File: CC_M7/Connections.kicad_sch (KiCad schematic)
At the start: 11 parts, among them J11 USB_B_Micro, J12 Conn_01x05_Pin, J16 Conn_01x06_Pin, J17 Conn_01x04_Pin, J3 Conn_01x03_Pin, J4 Conn_01x03_Pin, J5 Conn_01x03_Pin, J6 Conn_01x03_Pin, J7 Conn_01x03_Pin, J8 Conn_01x03_Pin

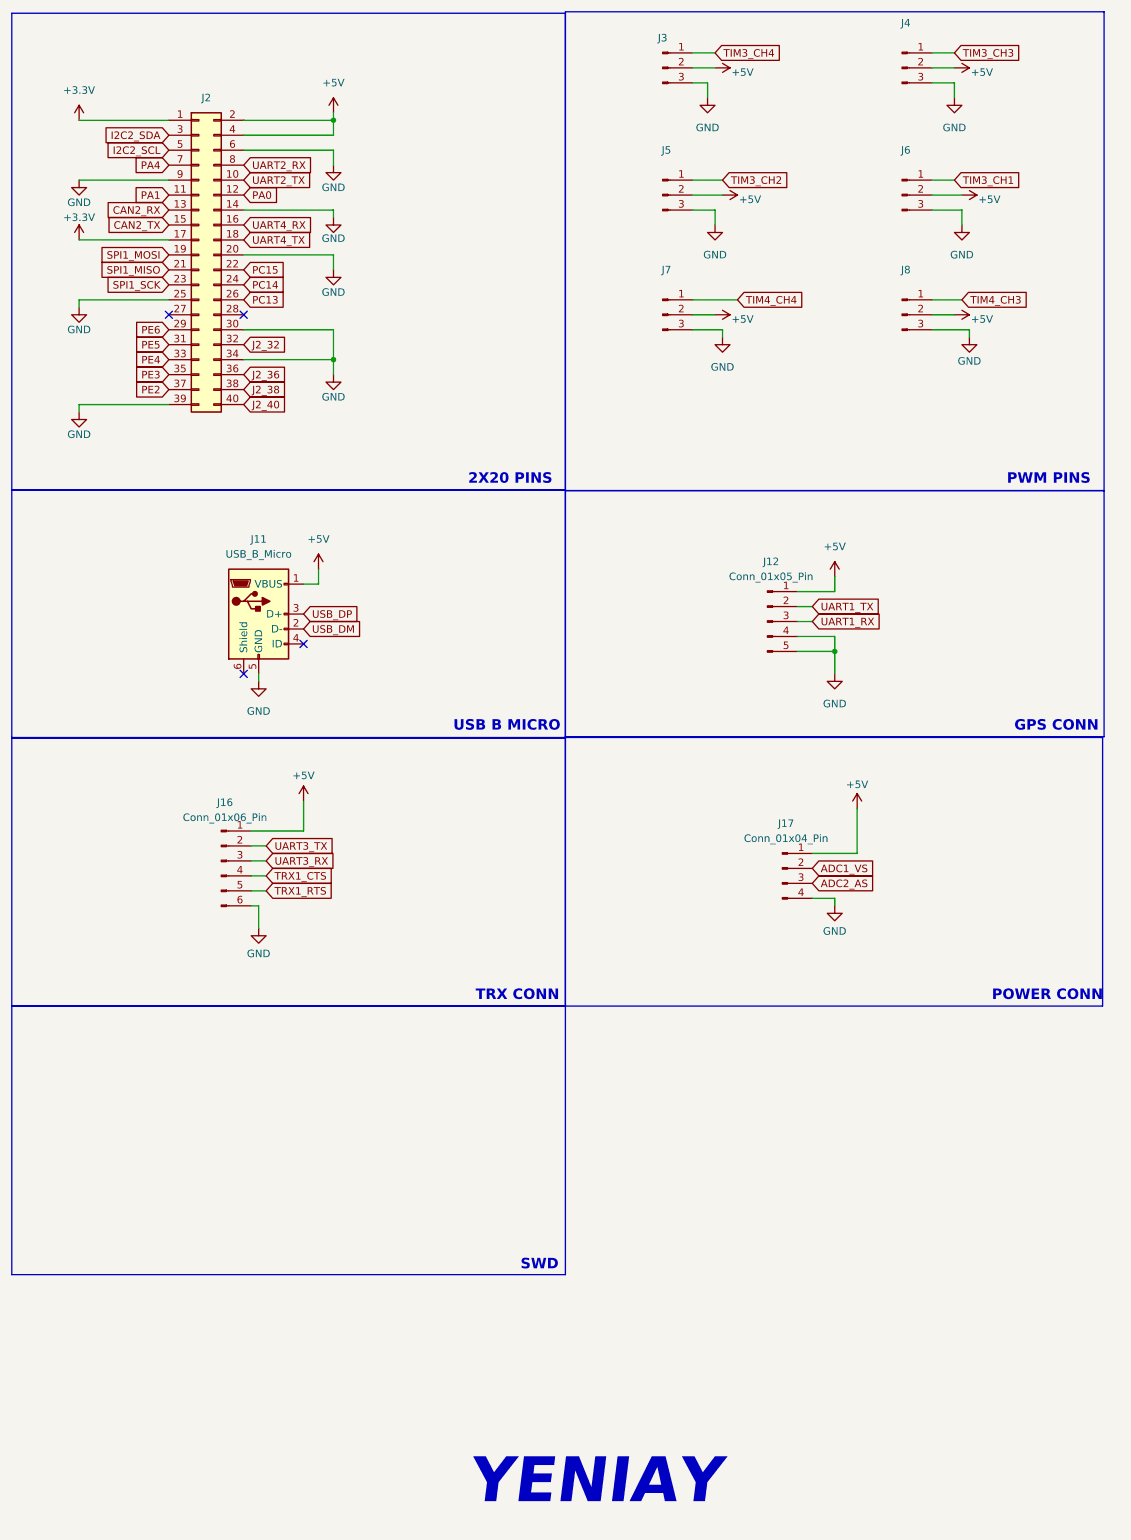
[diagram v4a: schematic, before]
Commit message: schematic control comment
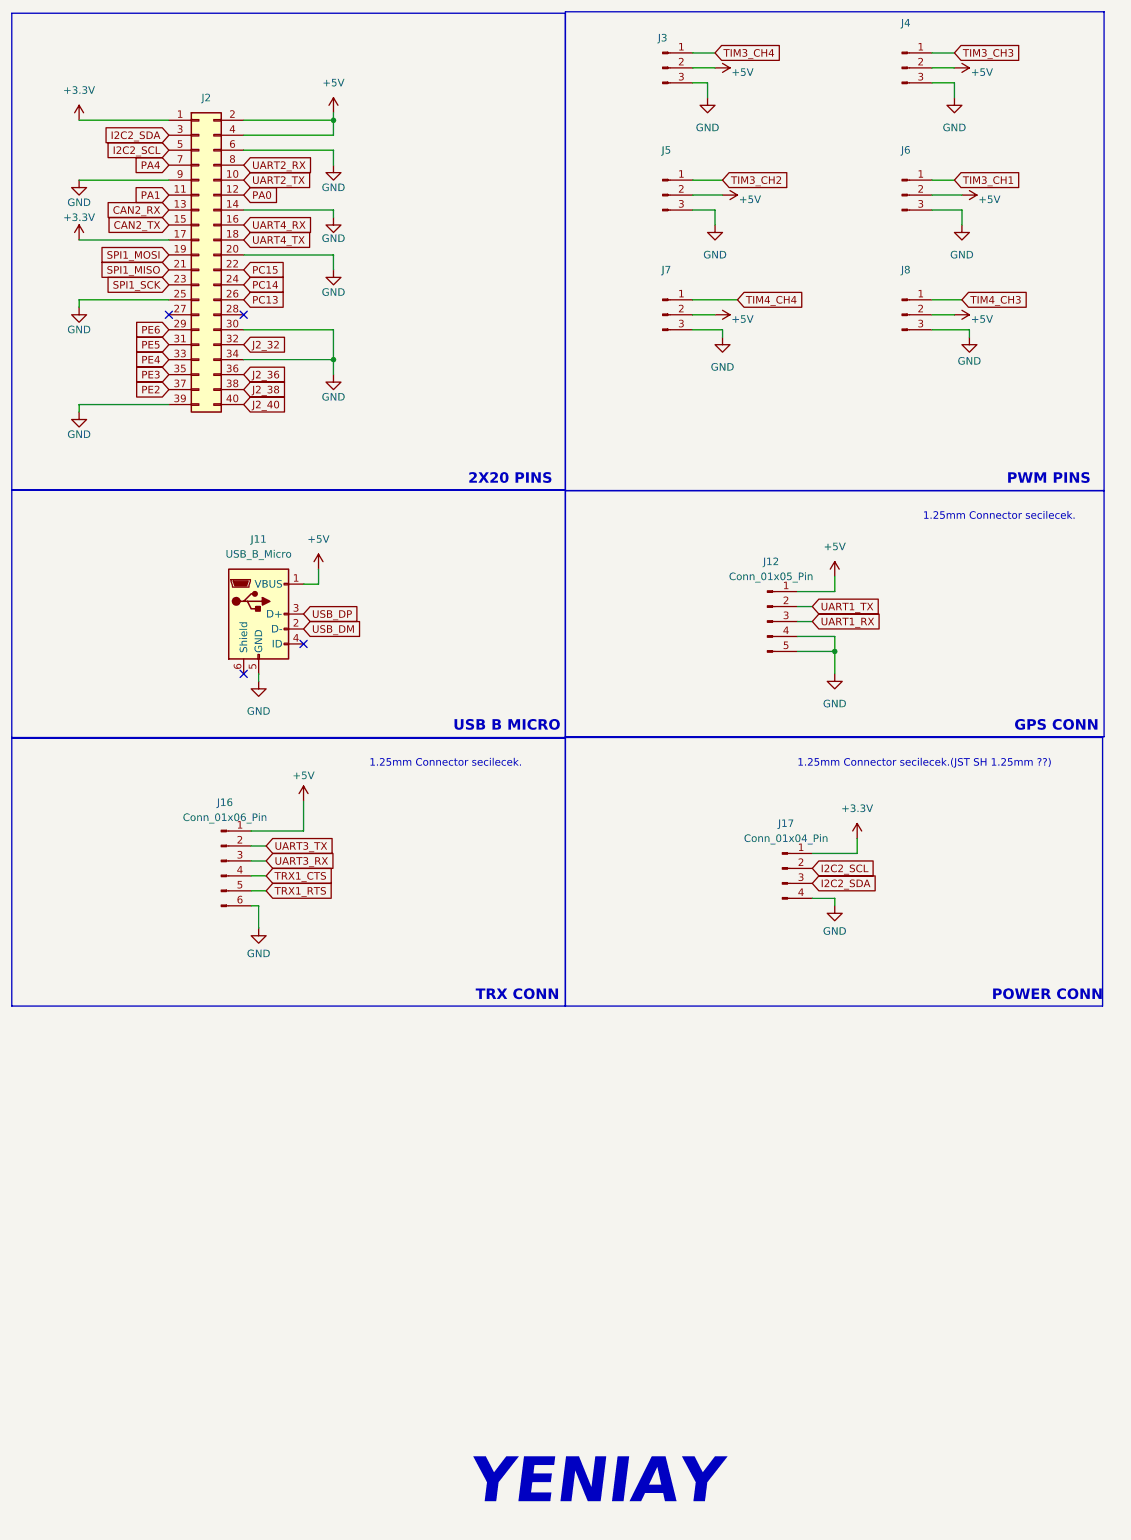
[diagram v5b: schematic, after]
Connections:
- net ADC1_VS is gone; now on net I2C2_SCL: J17.2 (Pin_2)
- net ADC2_AS is gone; now on net I2C2_SDA: J17.3 (Pin_3)
- net +3.3V: now also J17.1 (Pin_1)
- net +5V: no longer J17.1 (Pin_1)
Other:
- note added: "1.25mm Connector secilecek."
- note added: "1.25mm Connector secilecek.(JST SH 1.25mm ??)"
- note removed: "SWD"
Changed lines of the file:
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@@
 	(wire
 		(pts
-			(xy 156.21 154.94) (xy 156.21 147.32)
+			(xy 146.05 120.65) (xy 152.4 120.65)
 		)
 		(stroke
@@
 	(wire
 		(pts
-			(xy 146.05 120.65) (xy 152.4 120.65)
+			(xy 67.31 38.1) (xy 67.31 35.56)
 		)
 		(stroke
@@
 	(wire
 		(pts
-			(xy 67.31 38.1) (xy 67.31 35.56)
+			(xy 175.26 66.04) (xy 175.26 67.31)
 		)
 		(stroke
@@
 	(wire
 		(pts
-			(xy 175.26 66.04) (xy 175.26 67.31)
+			(xy 53.34 151.13) (xy 62.23 151.13)
 		)
 		(stroke
@@
 	(wire
 		(pts
-			(xy 53.34 151.13) (xy 62.23 151.13)
+			(xy 152.4 107.95) (xy 152.4 110.49)
 		)
 		(stroke
@@
 	(wire
 		(pts
-			(xy 152.4 107.95) (xy 152.4 110.49)
+			(xy 133.35 66.04) (xy 133.35 67.31)
 		)
 		(stroke
@@
 	(wire
 		(pts
-			(xy 133.35 66.04) (xy 133.35 67.31)
+			(xy 132.08 45.72) (xy 132.08 48.26)
 		)
 		(stroke
@@
 	(wire
 		(pts
-			(xy 132.08 45.72) (xy 132.08 48.26)
+			(xy 156.21 152.4) (xy 156.21 154.94)
 		)
 		(stroke
@@
 		)
 	)
-	(rectangle
-		(start 12.7 180.848)
-		(end 106.68 226.441)
-		(stroke
-			(width 0)
-			(type default)
-		)
-		(fill
-			(type none)
-		)
-	)
 	(text "YENIAY"
 		(exclude_from_sim no)
@@
 		)
 	)
-	(text "SWD\n"
+	(text "GPS CONN"
 		(exclude_from_sim no)
-		(at 99.06 224.79 0)
+		(at 182.88 133.35 0)
 		(effects
 			(font
@@
 		)
 	)
-	(text "GPS CONN"
+	(text "1.25mm Connector secilecek."
 		(exclude_from_sim no)
-		(at 182.88 133.35 0)
+		(at 180.34 97.79 0)
 		(effects
 			(font
-				(size 1.778 1.778)
-				(thickness 0.3556)
-				(bold yes)
+				(size 1.27 1.27)
 			)
-			(justify left)
 		)
 	)
@@
 		)
 	)
+	(text "1.25mm Connector secilecek."
+		(exclude_from_sim no)
+		(at 86.36 139.7 0)
+		(effects
+			(font
+				(size 1.27 1.27)
+			)
+		)
+	)
+	(text "1.25mm Connector secilecek.(JST SH 1.25mm ??)"
+		(exclude_from_sim no)
+		(at 167.64 139.7 0)
+		(effects
+			(font
+				(size 1.27 1.27)
+			)
+		)
+	)
 	(text "USB B MICRO"
 		(exclude_from_sim no)
@@
 		)
 	)
-	(global_label "UART1_RX"
+	(global_label "I2C2_SDA"
 		(shape input)
-		(at 148.59 115.57 0)
+		(at 148.59 160.02 0)
 		(fields_autoplaced yes)
 		(effects
@@
 		)
 		(property "Intersheetrefs" "${INTERSHEET_REFS}"
-			(at 160.8885 115.57 0)
+			(at 160.4047 160.02 0)
 			(effects
 				(font
@@
 		)
 	)
-	(global_label "PA4"
+	(global_label "UART1_RX"
 		(shape input)
-		(at 39.37 38.1 180)
+		(at 148.59 115.57 0)
 		(fields_autoplaced yes)
 		(effects
@@
 				(size 1.27 1.27)
 			)
-			(justify right)
+			(justify left)
 		)
 		(property "Intersheetrefs" "${INTERSHEET_REFS}"
-			(at 32.8167 38.1 0)
+			(at 160.8885 115.57 0)
 			(effects
 				(font
 					(size 1.27 1.27)
 				)
-				(justify right)
+				(justify left)
 				(hide yes)
 			)
 		)
 	)
-	(global_label "ADC1_VS"
+	(global_label "PA4"
 		(shape input)
-		(at 148.59 157.48 0)
+		(at 39.37 38.1 180)
 		(fields_autoplaced yes)
 		(effects
@@
 				(size 1.27 1.27)
 			)
-			(justify left)
+			(justify right)
 		)
 		(property "Intersheetrefs" "${INTERSHEET_REFS}"
-			(at 159.679 157.48 0)
+			(at 32.8167 38.1 0)
 			(effects
 				(font
 					(size 1.27 1.27)
 				)
-				(justify left)
+				(justify right)
 				(hide yes)
 			)
@@
 		)
 	)
-	(global_label "ADC2_AS"
-		(shape input)
-		(at 148.59 160.02 0)
-		(fields_autoplaced yes)
-		(effects
-			(font
-				(size 1.27 1.27)
-			)
-			(justify left)
-		)
-		(property "Intersheetrefs" "${INTERSHEET_REFS}"
-			(at 159.679 160.02 0)
-			(effects
-				(font
-					(size 1.27 1.27)
-				)
-				(justify left)
-				(hide yes)
-			)
-		)
-	)
 	(global_label "TIM3_CH1"
 		(shape input)
@@
 		)
 	)
+	(global_label "I2C2_SCL"
+		(shape input)
+		(at 148.59 157.48 0)
+		(fields_autoplaced yes)
+		(effects
+			(font
+				(size 1.27 1.27)
+			)
+			(justify left)
+		)
+		(property "Intersheetrefs" "${INTERSHEET_REFS}"
+			(at 160.3442 157.48 0)
+			(effects
+				(font
+					(size 1.27 1.27)
+				)
+				(justify left)
+				(hide yes)
+			)
+		)
+	)
 	(global_label "UART2_TX"
 		(shape input)
@@
 	)
 	(symbol
+		(lib_id "power:+3.3V")
+		(at 156.21 152.4 0)
+		(unit 1)
+		(exclude_from_sim no)
+		(in_bom yes)
+		(on_board yes)
+		(dnp no)
+		(fields_autoplaced yes)
+		(property "Reference" "#PWR028"
+			(at 156.21 156.21 0)
+			(effects
+				(font
+					(size 1.27 1.27)
+				)
+				(hide yes)
+			)
+		)
+		(property "Value" "+3.3V"
+			(at 156.21 147.32 0)
+			(effects
+				(font
+					(size 1.27 1.27)
+				)
+			)
+		)
+		(property "Footprint" ""
+			(at 156.21 152.4 0)
+			(effects
+				(font
+					(size 1.27 1.27)
+				)
+				(hide yes)
+			)
+		)
+		(property "Datasheet" ""
+			(at 156.21 152.4 0)
+			(effects
+				(font
+					(size 1.27 1.27)
+				)
+				(hide yes)
+			)
+		)
+		(property "Description" "Power symbol creates a global label with name \"+3.3V\""
+			(at 156.21 152.4 0)
+			(effects
+				(font
+					(size 1.27 1.27)
+				)
+				(hide yes)
+			)
+		)
+		(pin "1"
+		)
+		(instances
+			(project "CC_M7"
+				(path "/20c3bbae-00c6-470e-8b69-dc0f665257a3/8b74e690-9be2-433b-8a0a-5eb3a275b61f"
+					(reference "#PWR028")
+					(unit 1)
+				)
+			)
+		)
+	)
+	(symbol
 		(lib_id "power:GND")
 		(at 173.99 48.26 0)
@@
 					(unit 1)
 				)
-			)
-		)
-	)
-	(symbol
-		(lib_id "power:+5V")
-		(at 156.21 147.32 0)
-		(unit 1)
-		(exclude_from_sim no)
-		(in_bom yes)
-		(on_board yes)
-		(dnp no)
-		(property "Reference" "#PWR091"
-			(at 156.21 151.13 0)
-			(effects
-				(font
-					(size 1.27 1.27)
-				)
-				(hide yes)
-			)
-		)
-		(property "Value" "+5V"
-			(at 156.21 143.256 0)
-			(effects
-				(font
-					(size 1.27 1.27)
-				)
-			)
-		)
-		(property "Footprint" ""
-			(at 156.21 147.32 0)
-			(effects
-				(font
-					(size 1.27 1.27)
-				)
-				(hide yes)
-			)
-		)
-		(property "Datasheet" ""
-			(at 156.21 147.32 0)
-			(effects
-				(font
-					(size 1.27 1.27)
-				)
-				(hide yes)
-			)
-		)
-		(property "Description" "Power symbol creates a global label with name \"+5V\""
-			(at 156.21 147.32 0)
-			(effects
-				(font
-					(size 1.27 1.27)
-				)
-				(hide yes)
-			)
-		)
-		(pin "1"
-		)
-		(instances
-			(project "CC_M7"
-				(path "/20c3bbae-00c6-470e-8b69-dc0f665257a3/8b74e690-9be2-433b-8a0a-5eb3a275b61f"
-					(reference "#PWR091")
-					(unit 1)
-				)

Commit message: Changes updated @ CCM7.docx
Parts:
- removed J12: Conn_01x05_Pin, symbol Connector:Conn_01x05_Pin
- removed J16: Conn_01x06_Pin, symbol Connector:Conn_01x06_Pin
- removed J17: Conn_01x04_Pin, symbol Connector:Conn_01x04_Pin
- added J1, J10, J12: Conn_01x04_Pin, symbol Connector:Conn_01x04_Pin
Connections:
- net +5V: now also J10.1 (Pin_1), J12.1 (Pin_1)
- net GND: now also J1.4 (Pin_4), J10.4 (Pin_4), J12.4 (Pin_4)
- net UART1_RX: now also J10.3 (Pin_3)
- net UART1_TX: now also J10.2 (Pin_2)
- net UART3_RX: now also J12.3 (Pin_3)
- net UART3_TX: now also J12.2 (Pin_2)
- new net I2C1_SCL: J1.3 (Pin_3)
- new net I2C1_SDA: J1.2 (Pin_2)
- new net VIN: J1.1 (Pin_1)
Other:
- note added: "*2A dayanıklı connector secilecek."
- moved on the sheet: J2, J3, J4, J5, J6, J7, J8

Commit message: assigned footprint completed
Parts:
- J1, J10, J12: footprint (none) -> Connector_PinHeader_1.27mm:PinHeader_1x04_P1.27mm_Vertical
- J11: footprint (none) -> Connector_USB:USB_Micro-B_Wuerth_629105150521
- J2: footprint (none) -> Connector_IDC:IDC-Header_2x20_P2.54mm_Vertical
- J3, J4, J5, J6, J7, J8: footprint (none) -> Connector_PinHeader_2.54mm:PinHeader_1x03_P2.54mm_Vertical
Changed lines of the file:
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@@
 			)
 		)
-		(property "Footprint" ""
+		(property "Footprint" "Connector_PinHeader_2.54mm:PinHeader_1x03_P2.54mm_Vertical"
 			(at 123.19 71.12 0)
 			(effects
@@
 			)
 		)
-		(property "Footprint" ""
+		(property "Footprint" "Connector_IDC:IDC-Header_2x20_P2.54mm_Vertical"
 			(at 55.88 52.07 0)
 			(effects
@@
 			)
 		)
-		(property "Footprint" ""
+		(property "Footprint" "Connector_PinHeader_2.54mm:PinHeader_1x03_P2.54mm_Vertical"
 			(at 163.83 29.21 0)
 			(effects
@@
 			)
 		)
-		(property "Footprint" ""
+		(property "Footprint" "Connector_PinHeader_2.54mm:PinHeader_1x03_P2.54mm_Vertical"
 			(at 123.19 50.8 0)
 			(effects
@@
 			)
 		)
-		(property "Footprint" ""
+		(property "Footprint" "Connector_PinHeader_1.27mm:PinHeader_1x04_P1.27mm_Vertical"
 			(at 143.51 158.75 0)
 			(effects
@@
 			)
 		)
-		(property "Footprint" ""
+		(property "Footprint" "Connector_USB:USB_Micro-B_Wuerth_629105150521"
 			(at 58.42 115.57 0)
 			(effects
@@
 			)
 		)
-		(property "Footprint" ""
+		(property "Footprint" "Connector_PinHeader_2.54mm:PinHeader_1x03_P2.54mm_Vertical"
 			(at 163.83 71.12 0)
 			(effects
@@
 			)
 		)
-		(property "Footprint" ""
+		(property "Footprint" "Connector_PinHeader_2.54mm:PinHeader_1x03_P2.54mm_Vertical"
 			(at 123.19 29.21 0)
 			(effects
@@
 			)
 		)
-		(property "Footprint" ""
+		(property "Footprint" "Connector_PinHeader_2.54mm:PinHeader_1x03_P2.54mm_Vertical"
 			(at 163.83 50.8 0)
 			(effects
@@
 			)
 		)
-		(property "Footprint" ""
+		(property "Footprint" "Connector_PinHeader_1.27mm:PinHeader_1x04_P1.27mm_Vertical"
 			(at 52.07 156.21 0)
 			(effects
@@
 			)
 		)
-		(property "Footprint" ""
+		(property "Footprint" "Connector_PinHeader_1.27mm:PinHeader_1x04_P1.27mm_Vertical"
 			(at 140.97 113.03 0)
 			(effects

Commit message: ready to start PCB drawing
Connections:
- net VIN renamed +BATT
